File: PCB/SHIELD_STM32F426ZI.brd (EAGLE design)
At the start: 100 x 118.1 mm, 2 parts, among them IC1 AS4C16M16SA-6TCN

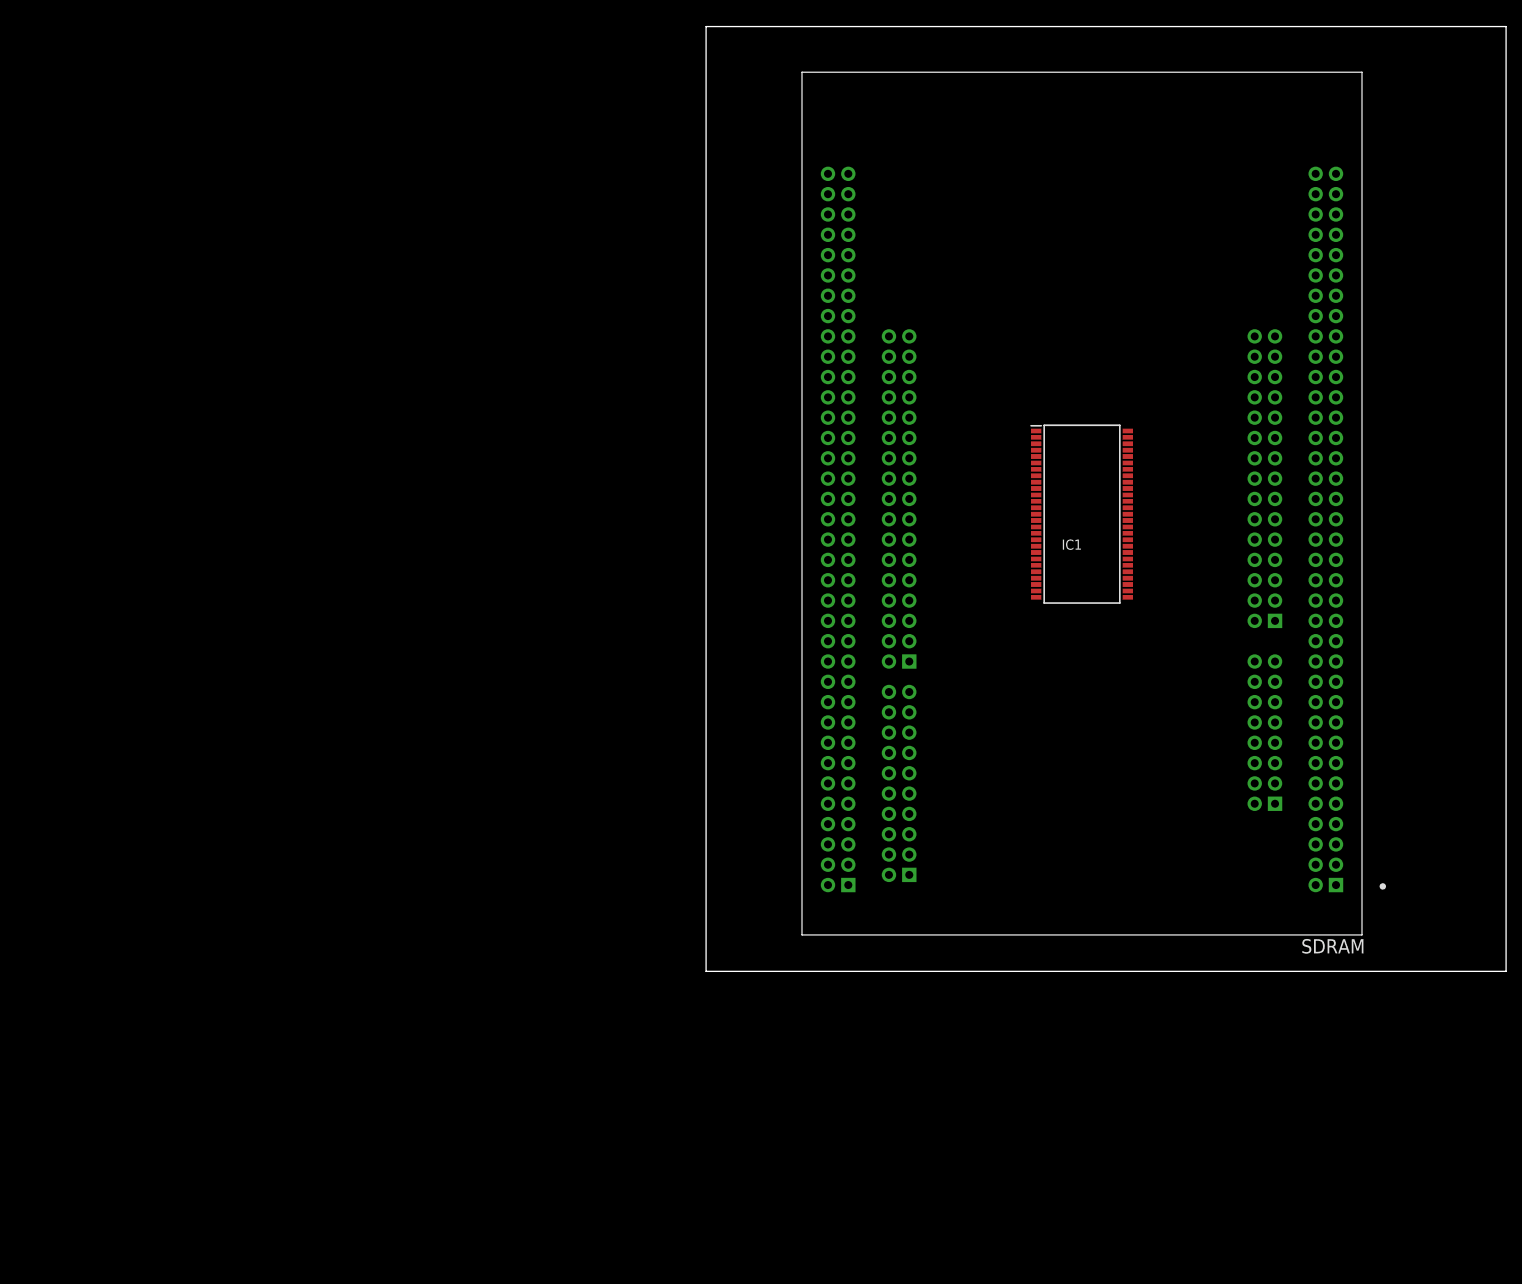
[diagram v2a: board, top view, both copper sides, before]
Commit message: new with sdramm and sdcard
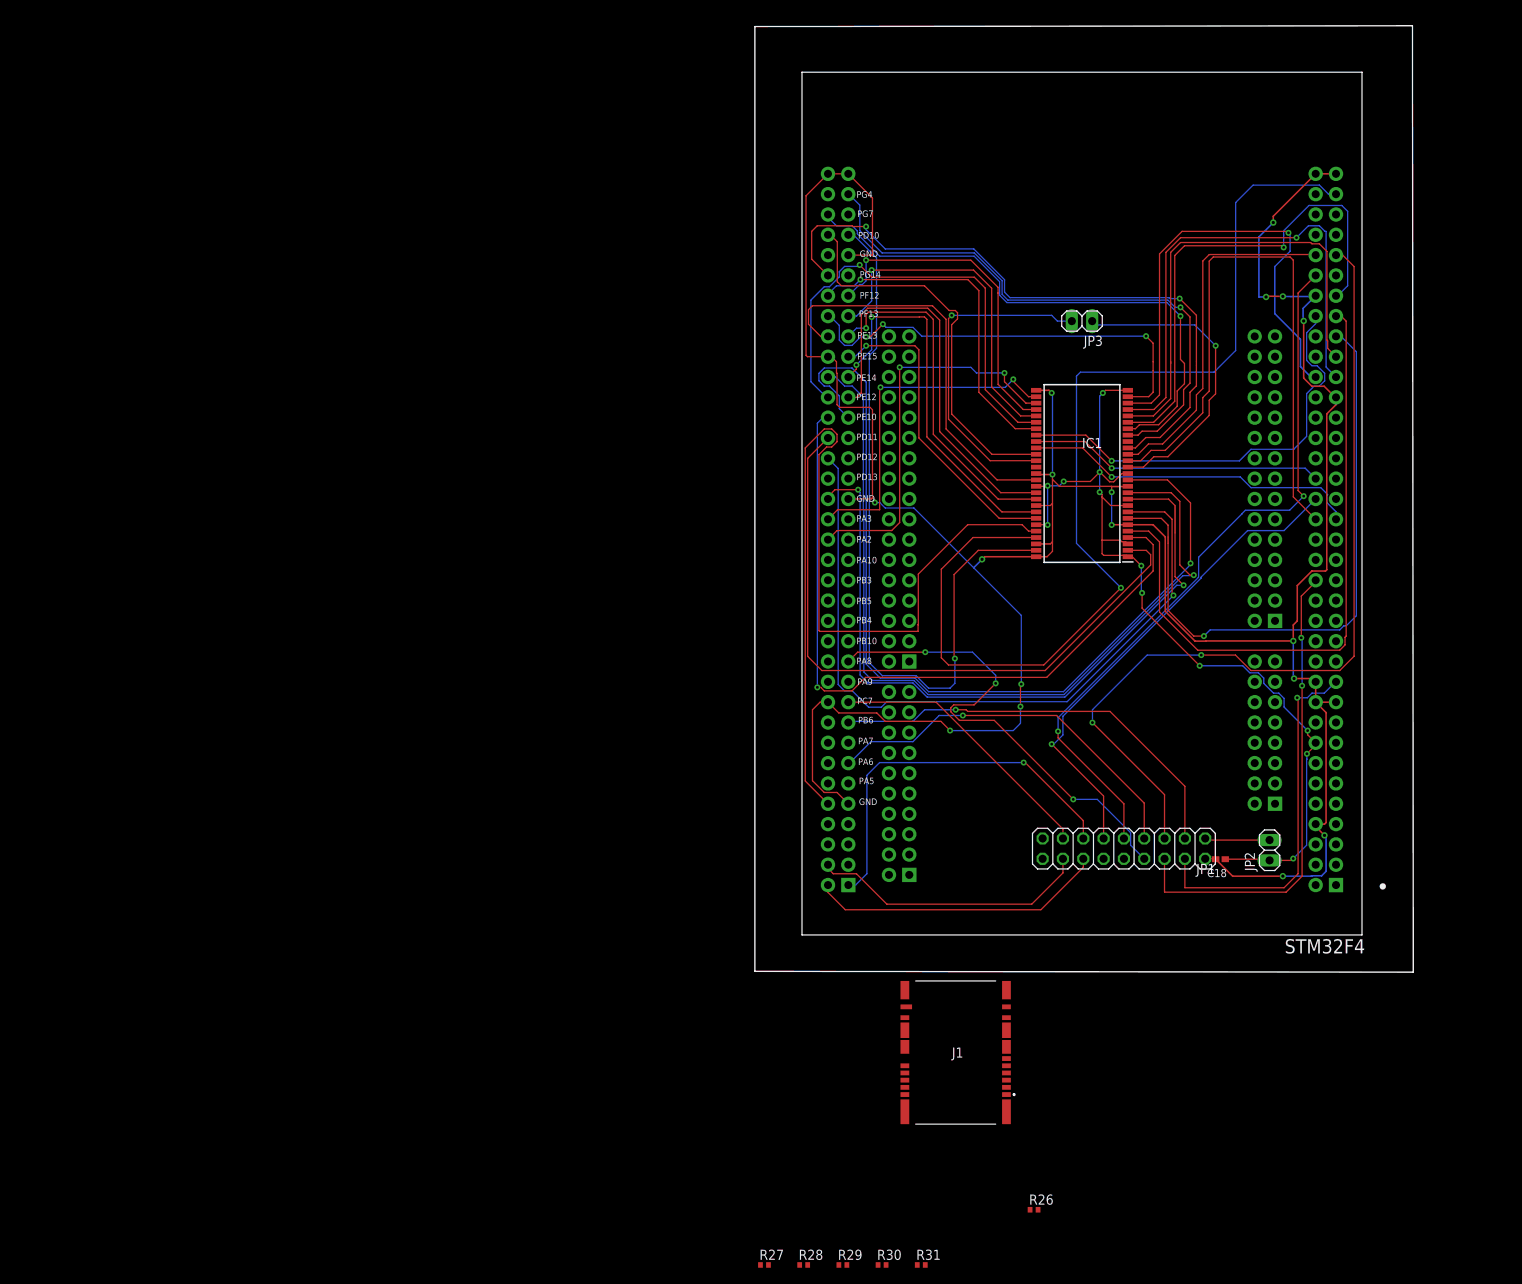
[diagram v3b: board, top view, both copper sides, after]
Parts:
- added C18: 0.1uF, rcl:C0402K
- added J1: 104239-1430, SamacSys_Parts:1042391430
- added JP1: (no value), pinhead:2X09
- added JP2, JP3: (no value), pinhead:1X02
- added R26, R27, R28, R29, R30, R31: 100k, rcl:R0402
- moved IC1 5.08 mm to (47.0, 62.2), turned to 180 degrees
- renumbered SDRAM to STM32F4
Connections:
- removed net N$1: IC1.1
- removed net N$101: STM32F4.CN11_58
- removed net N$102: STM32F4.CN11_59
- removed net N$104: STM32F4.CN11_62
- removed net N$105: STM32F4.CN11_63
- removed net N$113: STM32F4.CN12_13
- removed net N$117: STM32F4.CN12_17
- removed net N$119: STM32F4.CN12_19
- removed net N$12: IC1.12
- removed net N$122: STM32F4.CN12_23
- removed net N$14: IC1.14
- removed net N$15: IC1.15
- removed net N$22: STM32F4.CN12_1
- removed net N$24: STM32F4.CN11_2
- removed net N$26: IC1.27
- removed net N$27: IC1.54
- removed net N$29: IC1.52
- removed net N$3: IC1.3
- removed net N$32: IC1.49
- removed net N$35: IC1.46
- removed net N$38: IC1.43
- removed net N$40: IC1.41
- removed net N$42: IC1.39
- removed net N$45: STM32F4.CN12_2
- removed net N$46: STM32F4.CN12_3
- removed net N$47: STM32F4.CN12_4
- removed net N$52: STM32F4.CN12_20, STM32F4.CN12_39, STM32F4.CN12_54, STM32F4.CN12_63, STM32F4.CN12_71, STM32F4.CN12_72, STM32F4.CN12_9
- removed net N$53: IC1.28
- removed net N$6: IC1.6
- removed net N$64: STM32F4.CN11_16
- removed net N$67: STM32F4.CN11_19, STM32F4.CN11_20, STM32F4.CN11_22, STM32F4.CN11_49, STM32F4.CN11_60, STM32F4.CN11_71, STM32F4.CN11_72, STM32F4.CN11_8
- removed net N$68: STM32F4.CN11_21
- removed net N$77: STM32F4.CN11_32
- removed net N$85: STM32F4.CN11_40
- removed net N$87: STM32F4.CN11_42
- removed net N$9: IC1.9
- removed net N$93: STM32F4.CN11_48
- removed net N$94: STM32F4.CN11_50
- new net 3.3: JP1.1, JP2.2
- new net 3.3V: C18.1, IC1.1, IC1.14, IC1.27, IC1.3, IC1.43, IC1.49, IC1.9, JP2.1, R26.1, R27.1, R28.1, R29.1, R30.1, R31.1, STM32F4.CN11_16
- new net 3V3: J1.10
- new net CARD_DET: J1.23
- new net DCMI_D0: JP1.16, STM32F4.CN12_4
- new net DCMI_D1: JP1.15, STM32F4.CN12_19
- new net DCMI_D2: JP1.14, STM32F4.CN12_2
- new net DCMI_D3: JP1.13, STM32F4.CN12_1
- new net DCMI_D4: JP1.12, STM32F4.CN11_48
- new net DCMI_D5: JP1.11, STM32F4.CN11_40
- new net DCMI_D6: JP1.10, STM32F4.CN11_50
- new net DCMI_D7: JP1.9, STM32F4.CN11_62
- new net DCMI_HSYNC: JP1.6, STM32F4.CN11_32
- new net DCMI_PIXCK: JP1.7, STM32F4.CN12_13
- new net DCMI_VSYNC: JP1.5, STM32F4.CN11_63
- new net GND: C18.2, IC1.12, IC1.28, IC1.41, IC1.46, IC1.52, IC1.54, IC1.6, J1.12, J1.15, J1.16, J1.17, J1.18, J1.19, J1.20, J1.21, J1.22, JP1.2, STM32F4.CN11_19, STM32F4.CN11_20, STM32F4.CN11_22, STM32F4.CN11_49, STM32F4.CN11_60, STM32F4.CN11_71, STM32F4.CN11_72, STM32F4.CN11_8, STM32F4.CN12_20, STM32F4.CN12_39, STM32F4.CN12_54, STM32F4.CN12_63, STM32F4.CN12_71, STM32F4.CN12_72, STM32F4.CN12_9
- new net I2C1_SCL: JP1.3, STM32F4.CN12_17
- new net I2C1_SDA: JP1.4, STM32F4.CN11_21
- new net LDQM: IC1.15, JP3.1
- new net PWDN: JP1.18
- new net RCC_MCO_1: JP1.8, STM32F4.CN12_23
- new net RESET: JP1.17
- new net SDIO_CK: J1.11, R29.2
- new net SDIO_CMD: J1.9, R27.2
- new net SDIO_D0: J1.13, R28.2
- new net SDIO_D1: J1.14, R31.2
- new net SDIO_D2: J1.7, R26.2
- new net SDIO_D3: J1.8, R30.2
- new net UDQM: IC1.39, JP3.2
- net FMC_A10: now also STM32F4.CN11_59
- net FMC_A11: now also STM32F4.CN11_58
- net FMC_A12: now also STM32F4.CN11_42
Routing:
- net GND: track 0.00 -> 368.2 mm, vias 0 -> 17
- net FMC_D14: track 0.00 -> 133.8 mm, vias 0 -> 1
- net 3.3V: track 0.00 -> 115.3 mm, vias 0 -> 12
- net FMC_D7: track 0.00 -> 114.9 mm, vias 0 -> 1
- net FMC_D13: track 0.00 -> 114.0 mm
- net DCMI_VSYNC: track 0.00 -> 108.5 mm, vias 0 -> 2
- net FMC_D6: track 0.00 -> 105.6 mm, vias 0 -> 1
- net FMC_D4: track 0.00 -> 93.2 mm, vias 0 -> 1
- net FMC_D15: track 0.00 -> 93.1 mm, vias 0 -> 1
- net FMC_D5: track 0.00 -> 91.7 mm, vias 0 -> 2
- net DCMI_D7: track 0.00 -> 91.0 mm, vias 0 -> 2
- net FMC_D1: track 0.00 -> 89.8 mm, vias 0 -> 1
- net FMC_SDNRAS: track 0.00 -> 82.2 mm, vias 0 -> 2
- net FMC_D0: track 0.00 -> 81.8 mm
- net FMC_D2: track 0.00 -> 80.8 mm
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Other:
- board size 100 x 118.1 mm -> 82.3 x 118.3 mm
- board text added: "GND"
- board text added: "PA10"
- board text added: "PA2"
- board text added: "PA3"
- board text added: "PA5"
- board text added: "PA6"
- board text added: "PA7"
- board text added: "PA8"
- board text added: "PA9"
- board text added: "PB10"
- board text added: "PB3"
- board text added: "PB4"
- board text added: "PB5"
- board text added: "PB6"
- board text added: "PC7"
- board text added: "PD10"
- board text added: "PD11"
- board text added: "PD12"
- board text added: "PD13"
- board text added: "PE10"
- board text added: "PE12"
- board text added: "PE13"
- board text added: "PE14"
- board text added: "PE15"
- board text added: "PF12"
- board text added: "PF13"
- board text added: "PG14"
- board text added: "PG4"
- board text added: "PG7"

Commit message: neuste vision
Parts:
- added R1, R2: 4.7k, sicom_universal:C0402K
- moved R27 61.9 mm to (45.8, 11.8), turned to 90 degrees
- moved R28 61.5 mm to (50.1, 11.7), turned to 90 degrees
- moved R29 61.2 mm to (54.2, 12.0), turned to 90 degrees
- moved R30 60.7 mm to (58.0, 12.1), turned to 90 degrees
- moved R31 60.6 mm to (62.6, 12.2), turned to 90 degrees
- moved R26 49.3 mm to (67.3, 11.9), turned to 90 degrees
- moved J1 30.5 mm to (35.1, 11.2)
- moved JP1 13.5 mm to (55.6, 28.4)
- moved JP2 9.71 mm to (62.4, 20.6), turned to 180 degrees
- moved C18 4.24 mm to (67.1, 17.2), turned to 90 degrees
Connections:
- removed net N$103: STM32F4.CN11_61
- removed net N$111: STM32F4.CN11_70
- removed net N$160: STM32F4.CN12_64
- removed net N$23: STM32F4.CN11_1
- removed net N$25: STM32F4.CN11_3
- removed net N$54: STM32F4.CN11_4
- new net N$1: STM32F4.CN12_3
- net 3.3V: now also R1.2, R2.2
- net DCMI_D2: now also STM32F4.CN12_64; no longer STM32F4.CN12_2
- net DCMI_D3: now also STM32F4.CN11_61; no longer STM32F4.CN12_1
- net I2C1_SCL: now also R2.1
- net I2C1_SDA: now also R1.1
- net SDIO_CK: now also STM32F4.CN11_3
- net SDIO_CMD: now also STM32F4.CN11_4
- net SDIO_D0: now also STM32F4.CN12_2
- net SDIO_D1: now also STM32F4.CN12_1
- net SDIO_D2: now also STM32F4.CN11_1
- net SDIO_D3: now also STM32F4.CN11_2
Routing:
- net DCMI_D2: track 37.0 -> 118.0 mm
- net RCC_MCO_1: track 61.2 -> 0.00 mm, vias 3 -> 0
- net DCMI_HSYNC: track 60.0 -> 0.00 mm, vias 2 -> 0
- net FMC_D3: track 78.3 -> 21.9 mm
- net I2C1_SCL: track 53.2 -> 0.20 mm, vias 1 -> 0
- net I2C1_SDA: track 46.2 -> 0.05 mm, vias 1 -> 0
- net GND: track 368.2 -> 327.7 mm, vias 17 -> 15
- net DCMI_D3: track 48.2 -> 83.0 mm, vias 1 -> 0
- net DCMI_VSYNC: track 108.5 -> 78.8 mm, vias 2 -> 0
- net FMC_SDNWE: track 75.6 -> 50.3 mm
- net 3.3V: track 115.3 -> 92.1 mm, vias 12 -> 11
- net DCMI_D7: track 91.0 -> 72.0 mm, vias 2 -> 4
- net DCMI_D0: track 35.1 -> 50.8 mm
- net 3.3: track 8.13 -> 0.00 mm
- net FMC_A11: track 54.6 -> 50.1 mm, vias 1 -> 2
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
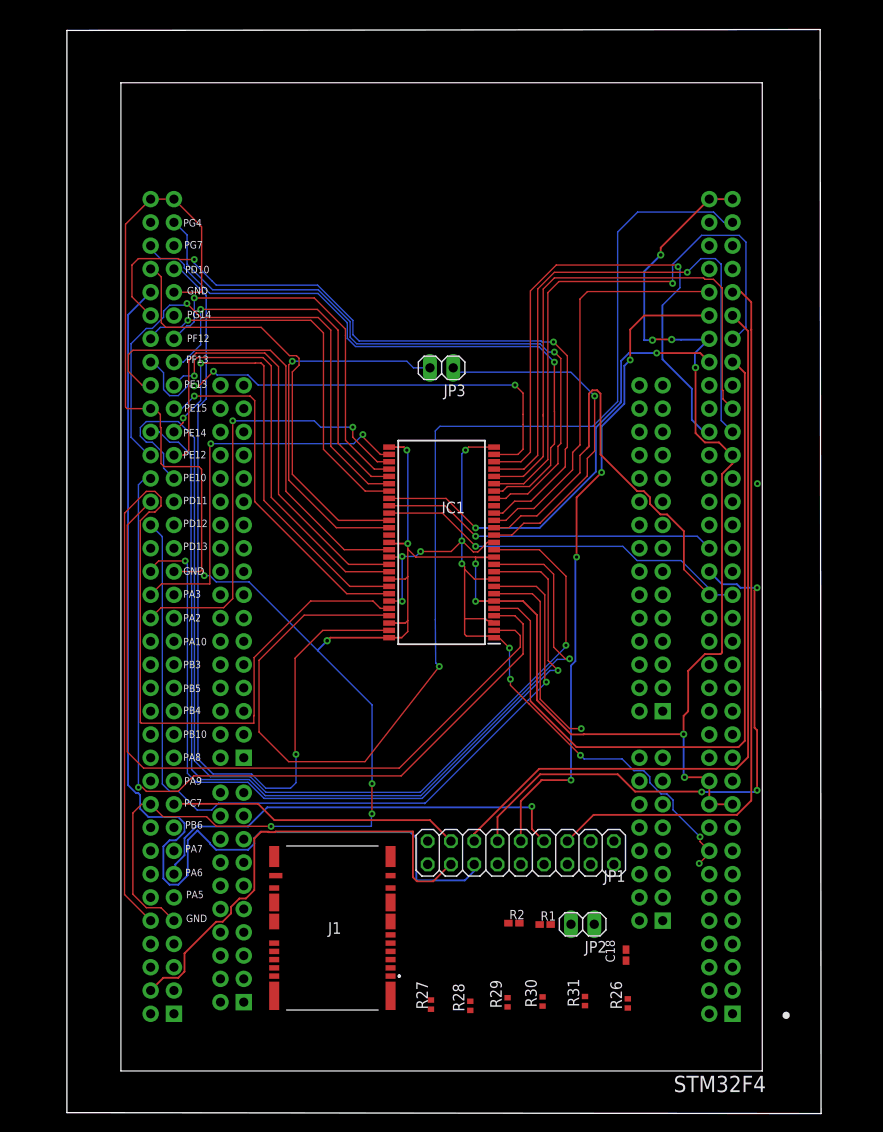
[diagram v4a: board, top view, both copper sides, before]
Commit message: sdcard wird hinzugefügt
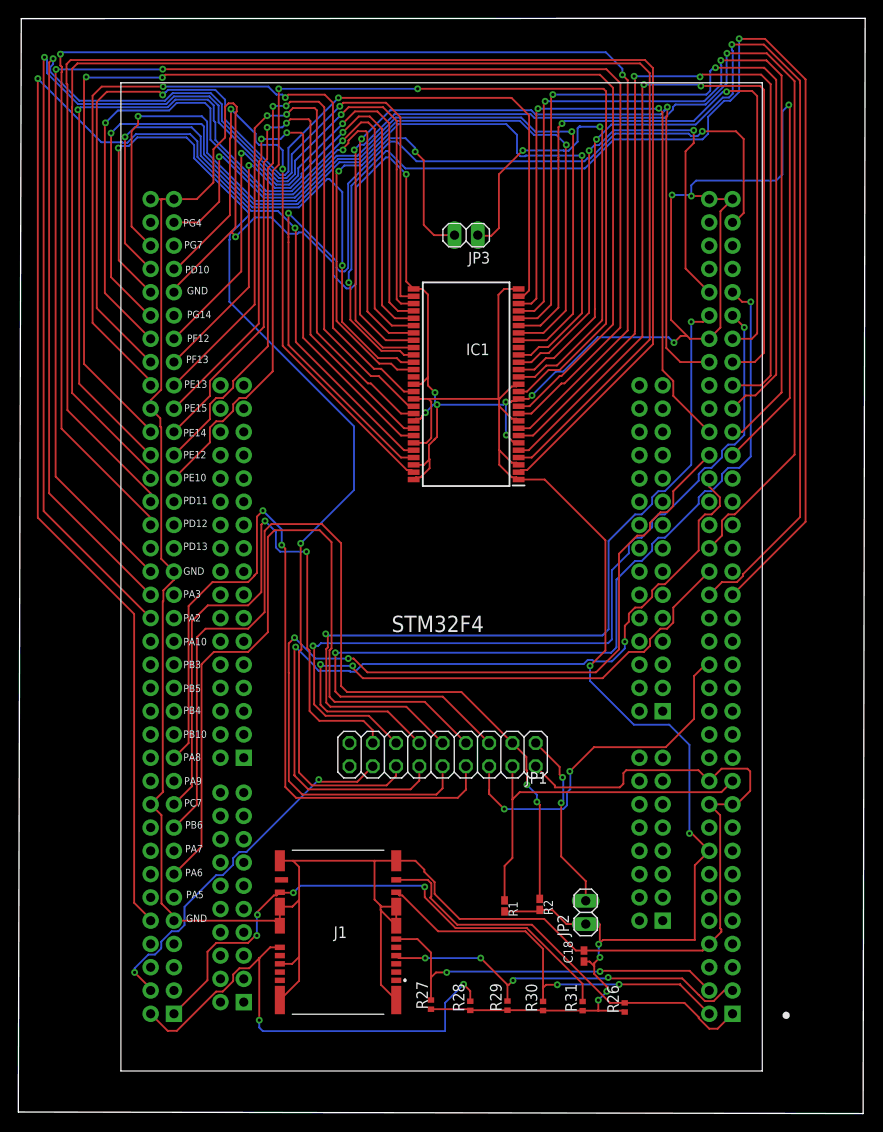
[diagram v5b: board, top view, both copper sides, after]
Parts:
- moved IC1 17.5 mm to (49.7, 79.5)
- moved JP3 14.7 mm to (49.7, 95.8)
- moved JP1 13.7 mm to (47.1, 39.1)
- moved R1 4.87 mm to (53.9, 22.6), turned to 270 degrees
- moved C18 4.59 mm to (62.5, 17.1)
- moved R2 3.49 mm to (57.7, 22.7), turned to 270 degrees
- moved JP2 1.33 mm to (62.7, 21.9), turned to 90 degrees
- moved J1 0.77 mm to (35.7, 10.7)
- moved R31 0.61 mm to (62.4, 11.6)
- moved R26 0.56 mm to (67.0, 11.5)
- moved R30 0.49 mm to (58.1, 11.6)
- moved R29 0.36 mm to (54.2, 11.7)
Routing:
- net GND: track 327.7 -> 503.1 mm, vias 15 -> 12
- net FMC_SDCKE0: track 41.2 -> 147.0 mm, vias 1 -> 2
- net I2C1_SCL: track 0.20 -> 103.8 mm, vias 0 -> 2
- net FMC_A12: track 36.9 -> 137.6 mm, vias 1 -> 2
- net DCMI_D6: track 0.00 -> 100.1 mm, vias 0 -> 2
- net DCMI_D4: track 0.20 -> 93.2 mm, vias 1 -> 2
- net FMC_A4: track 43.2 -> 135.8 mm
- net FMC_A5: track 48.8 -> 139.1 mm
- net RCC_MCO_1: track 0.00 -> 87.6 mm, vias 0 -> 2
- net FMC_D0: track 81.8 -> 166.7 mm
- net 3.3V: track 92.1 -> 168.3 mm, vias 11 -> 6
- net FMC_D3: track 21.9 -> 97.3 mm, vias 1 -> 2
- net FMC_SDNWE: track 50.3 -> 122.8 mm, vias 0 -> 2
- net FMC_D5: track 91.7 -> 163.0 mm
- net FMC_D1: track 89.8 -> 160.7 mm, vias 1 -> 0
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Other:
- board size 82.3 x 118.3 mm -> 92.4 x 119.5 mm

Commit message: neuster Stand
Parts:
- added R3: 10k, sicom_universal:C0402K
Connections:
- net N$1 renamed A
- removed net N$19: IC1.19
- net 3.3V: now also R3.2
- net FMC_SDNE0: now also IC1.19, R3.1
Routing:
- net FMC_SDNE0: track 0.00 -> 201.3 mm, vias 0 -> 2
- net 3.3V: track 168.3 -> 175.5 mm
- net FMC_SDNRAS: track 111.2 -> 111.9 mm
- added copper zone on layer 1, net GND

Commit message: modyfi gnd and Ratsnest
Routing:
- net GND: track 503.1 -> 0.00 mm, vias 12 -> 0
- net SDIO_D1: vias 4 -> 2
